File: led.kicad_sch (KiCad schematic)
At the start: 200 parts

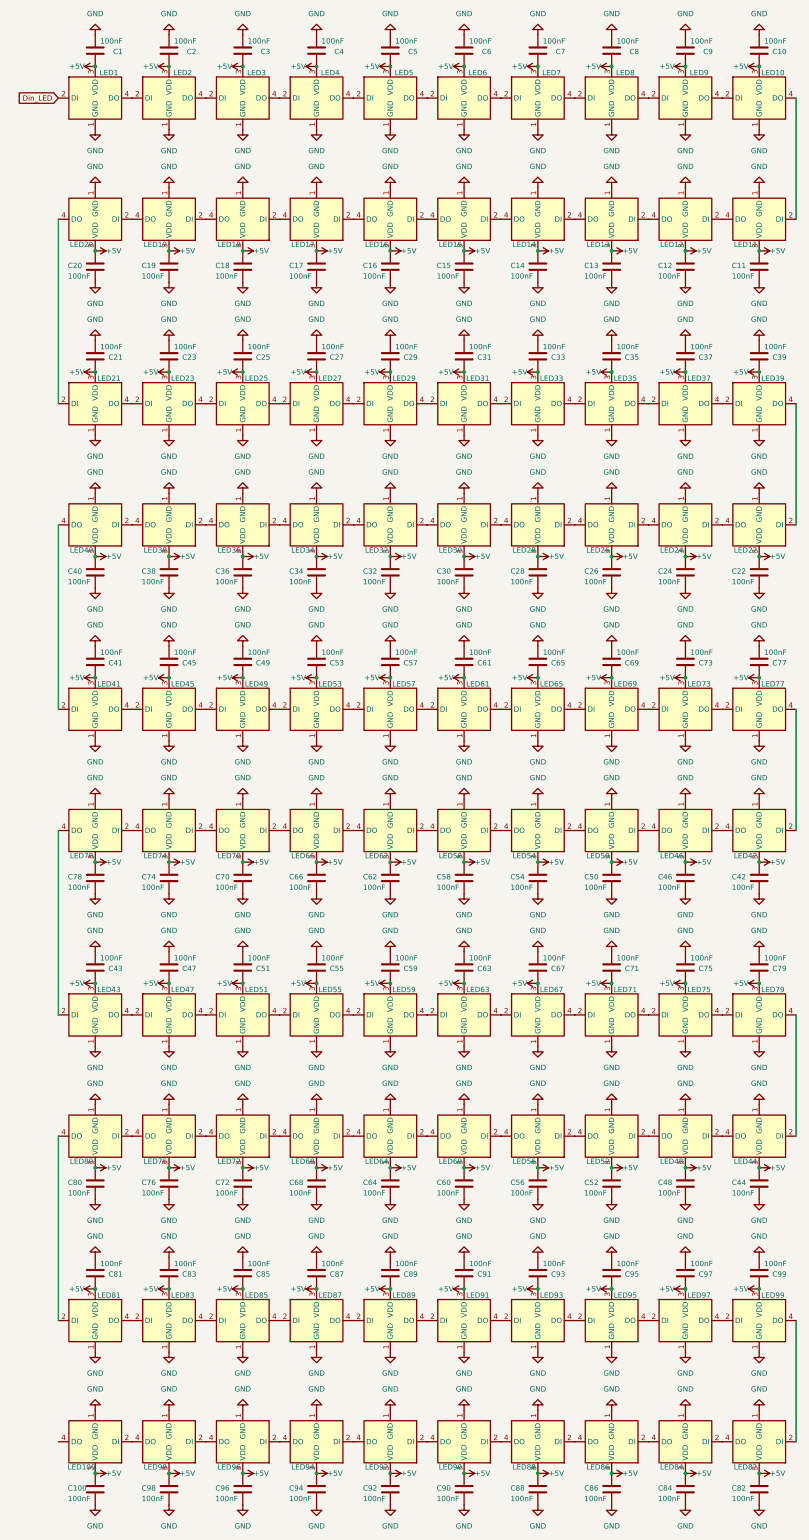
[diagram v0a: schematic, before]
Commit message: led verplaatst
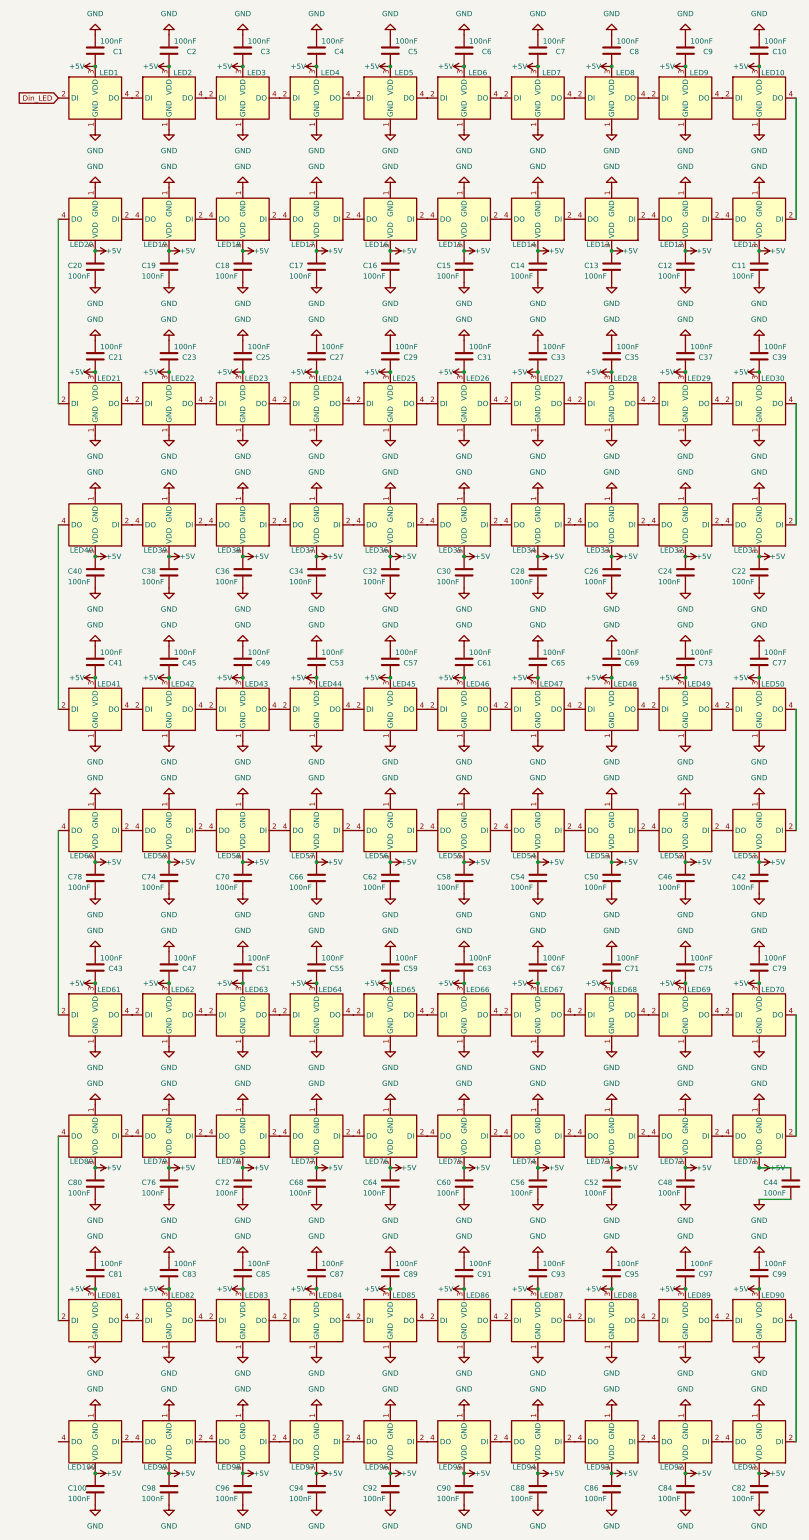
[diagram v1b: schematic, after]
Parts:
- renumbered LED23 to LED22, LED25 to LED23, LED27 to LED24, LED29 to LED25, LED31 to LED26, LED33 to LED27, LED35 to LED28, LED37 to LED29, LED39 to LED30, LED22 to LED31, LED24 to LED32, LED26 to LED33, LED28 to LED34, LED30 to LED35, LED32 to LED36, LED34 to LED37, LED36 to LED38, LED38 to LED39, LED45 to LED42, LED49 to LED43, LED53 to LED44, LED57 to LED45, LED61 to LED46, LED65 to LED47, LED69 to LED48, LED73 to LED49, LED77 to LED50, LED42 to LED51, LED46 to LED52, LED50 to LED53, LED58 to LED55, LED62 to LED56, LED66 to LED57, LED70 to LED58, LED74 to LED59, LED78 to LED60, LED43 to LED61, LED47 to LED62, LED51 to LED63, LED55 to LED64, LED59 to LED65, LED63 to LED66, LED71 to LED68, LED75 to LED69, LED79 to LED70, LED44 to LED71, LED48 to LED72, LED52 to LED73, LED56 to LED74, LED60 to LED75, LED64 to LED76, LED68 to LED77, LED72 to LED78, LED76 to LED79, LED83 to LED82, LED85 to LED83, LED87 to LED84, LED89 to LED85, LED91 to LED86, LED93 to LED87, LED95 to LED88, LED97 to LED89, LED99 to LED90, LED82 to LED91, LED84 to LED92, LED86 to LED93, LED88 to LED94, LED90 to LED95, LED92 to LED96, LED94 to LED97, LED96 to LED98, LED98 to LED99
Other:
- moved on the sheet: C44

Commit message: i fixed the layout
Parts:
- renumbered LED91 to LED100, LED20 to LED11, LED19 to LED12, LED18 to LED13, LED17 to LED14, LED16 to LED15, LED15 to LED16, LED14 to LED17, LED13 to LED18, LED12 to LED19, LED11 to LED20, LED40 to LED31, LED39 to LED32, LED38 to LED33, LED37 to LED34, LED36 to LED35, LED35 to LED36, LED34 to LED37, LED33 to LED38, LED32 to LED39, LED31 to LED40, LED60 to LED51, LED59 to LED52, LED58 to LED53, LED57 to LED54, LED56 to LED55, LED55 to LED56, LED54 to LED57, LED53 to LED58, LED52 to LED59, LED51 to LED60, LED80 to LED71, LED79 to LED72, LED78 to LED73, LED77 to LED74, LED76 to LED75, LED75 to LED76, LED74 to LED77, LED73 to LED78, LED72 to LED79, LED71 to LED80, LED100 to LED91, LED99 to LED92, LED98 to LED93, LED97 to LED94, LED96 to LED95, LED95 to LED96, LED94 to LED97, LED93 to LED98, LED92 to LED99
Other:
- moved on the sheet: C44
